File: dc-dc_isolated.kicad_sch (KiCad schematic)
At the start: 11 parts, among them U201 CMP6793RE

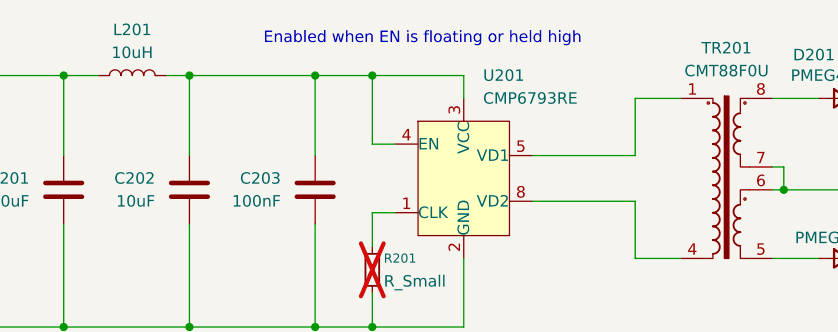
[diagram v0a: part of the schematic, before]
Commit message: no erc errors
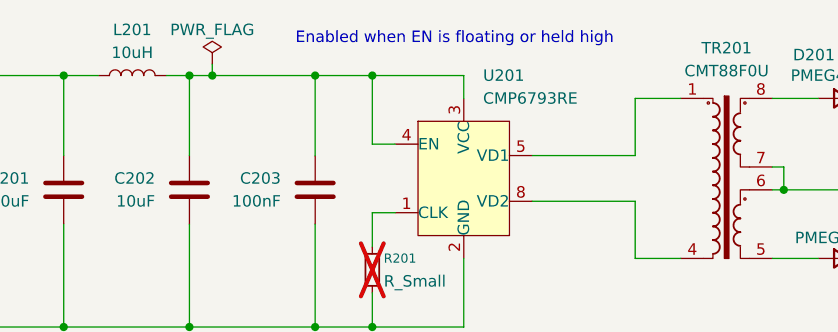
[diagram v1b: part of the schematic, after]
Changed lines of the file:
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@@
 	(text "Enabled when EN is floating or held high"
 		(exclude_from_sim no)
-		(at 74.168 81.026 0)
+		(at 77.724 81.026 0)
 		(effects
 			(font
@@
 	)
 	(junction
+		(at 50.8 85.09)
+		(diameter 0)
+		(color 0 0 0 0)
+	)
+	(junction
 		(at 143.51 97.79)
 		(diameter 0)
@@
 	(wire
 		(pts
+			(xy 50.8 85.09) (xy 62.23 85.09)
+		)
+		(stroke
+			(width 0)
+			(type default)
+		)
+	)
+	(wire
+		(pts
 			(xy 113.03 87.63) (xy 118.11 87.63)
 		)
@@
 	(wire
 		(pts
-			(xy 48.26 85.09) (xy 62.23 85.09)
+			(xy 48.26 85.09) (xy 50.8 85.09)
 		)
 		(stroke
@@
 		(pts
 			(xy 62.23 85.09) (xy 68.58 85.09)
+		)
+		(stroke
+			(width 0)
+			(type default)
+		)
+	)
+	(wire
+		(pts
+			(xy 50.8 83.82) (xy 50.8 85.09)
 		)
 		(stroke
@@
 					(unit 1)
 				)
+			)
+		)
+	)
+	(symbol
+		(lib_id "power:PWR_FLAG")
+		(at 50.8 83.82 0)
+		(unit 1)
+		(body_style 1)
+		(exclude_from_sim no)
+		(in_bom yes)
+		(on_board yes)
+		(in_pos_files yes)
+		(dnp no)
+		(property "Reference" "#FLG0201"
+			(at 50.8 81.915 0)
+			(hide yes)
+			(show_name no)
+			(do_not_autoplace no)
+			(effects
+				(font
+					(size 1.27 1.27)
+				)
+			)
+		)
+		(property "Value" "PWR_FLAG"
+			(at 50.8 80.01 0)
+			(show_name no)
+			(do_not_autoplace no)
+			(effects
+				(font
+					(size 1.27 1.27)
+				)
+			)
+		)
+		(property "Footprint" ""
+			(at 50.8 83.82 0)
+			(hide yes)
+			(show_name no)
+			(do_not_autoplace no)
+			(effects
+				(font
+					(size 1.27 1.27)
+				)
+			)
+		)
+		(property "Datasheet" ""
+			(at 50.8 83.82 0)
+			(hide yes)
+			(show_name no)
+			(do_not_autoplace no)
+			(effects
+				(font
+					(size 1.27 1.27)
+				)
+			)
+		)
+		(property "Description" "Special symbol for telling ERC where power comes from"
+			(at 50.8 83.82 0)
+			(hide yes)
+			(show_name no)
+			(do_not_autoplace no)
+			(effects
+				(font
+					(size 1.27 1.27)
+				)
+			)
+		)
+		(pin "1"
+		)
+		(instances
+			(project "Feeder"
+				(path "/8d0c1d66-35ef-4a53-a28f-436a11b54f42/0f88d378-7a6f-43ae-9bce-271f551b7098"
+					(reference "#FLG0301")
+					(unit 1)
+				)
+				(path "/8d0c1d66-35ef-4a53-a28f-436a11b54f42/e156698f-e6e2-4e2e-a060-ba71eca2a1f2"
+					(reference "#FLG0201")
+					(unit 1)
+				)
